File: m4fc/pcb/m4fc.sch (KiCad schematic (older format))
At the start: 70 parts

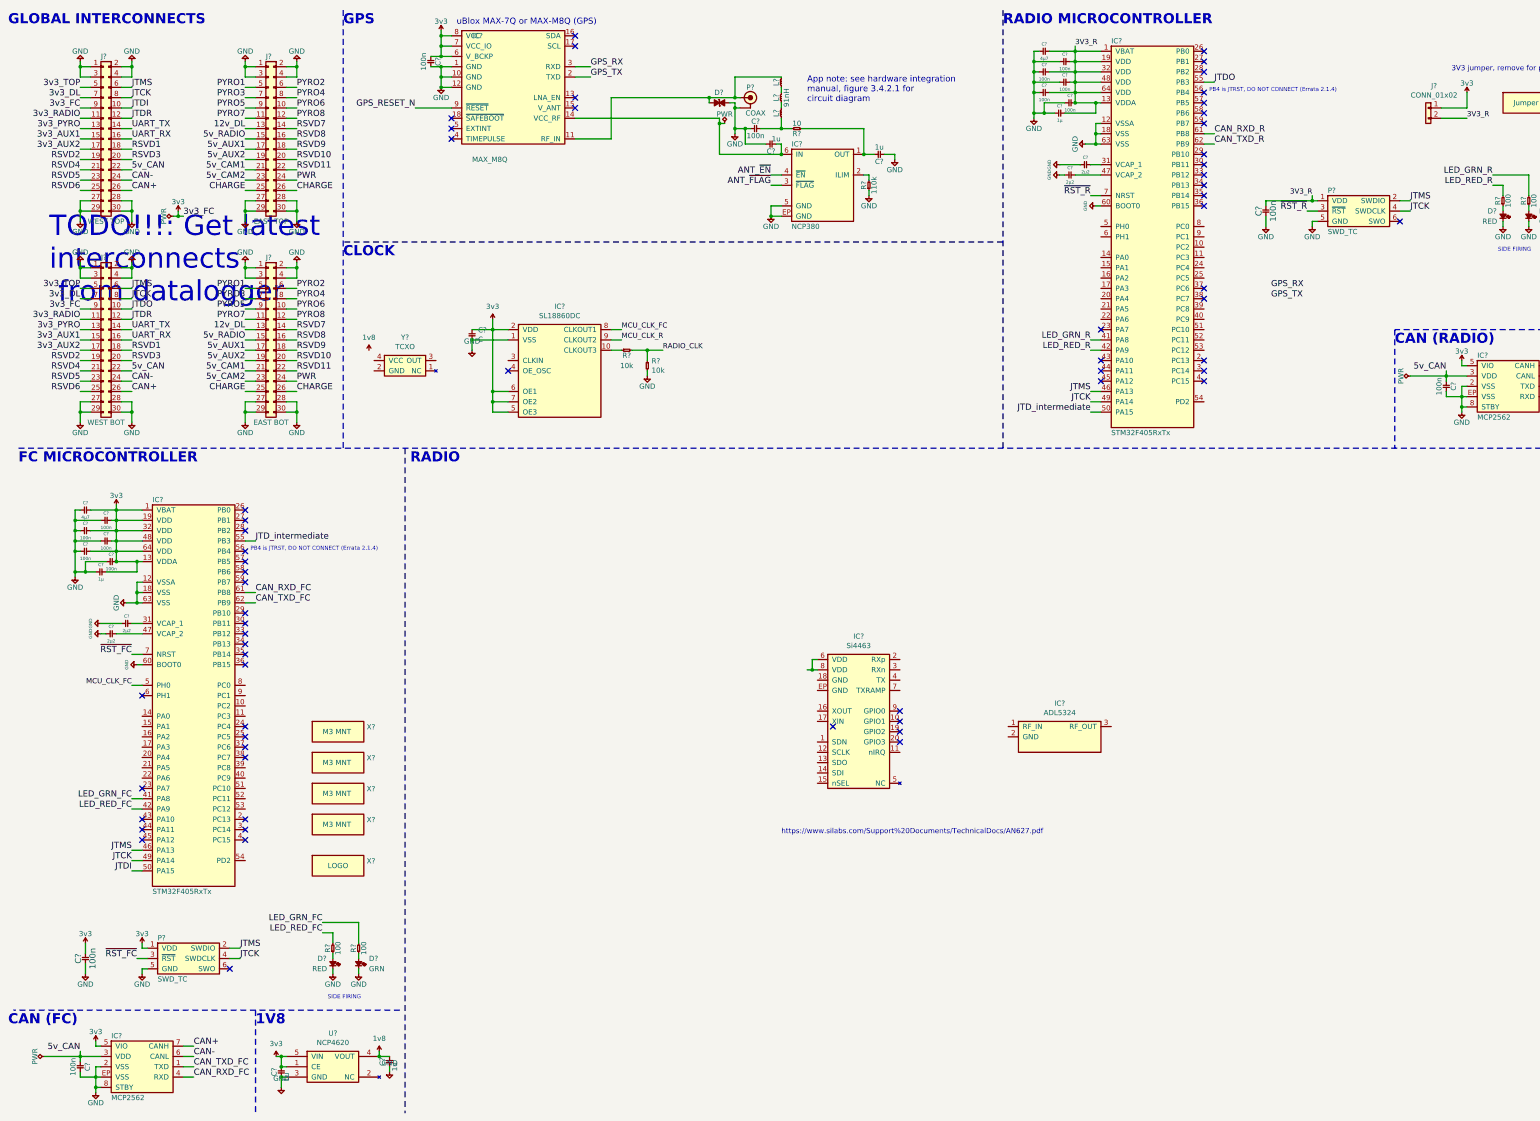
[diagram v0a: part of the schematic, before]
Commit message: Add FC components to schematic
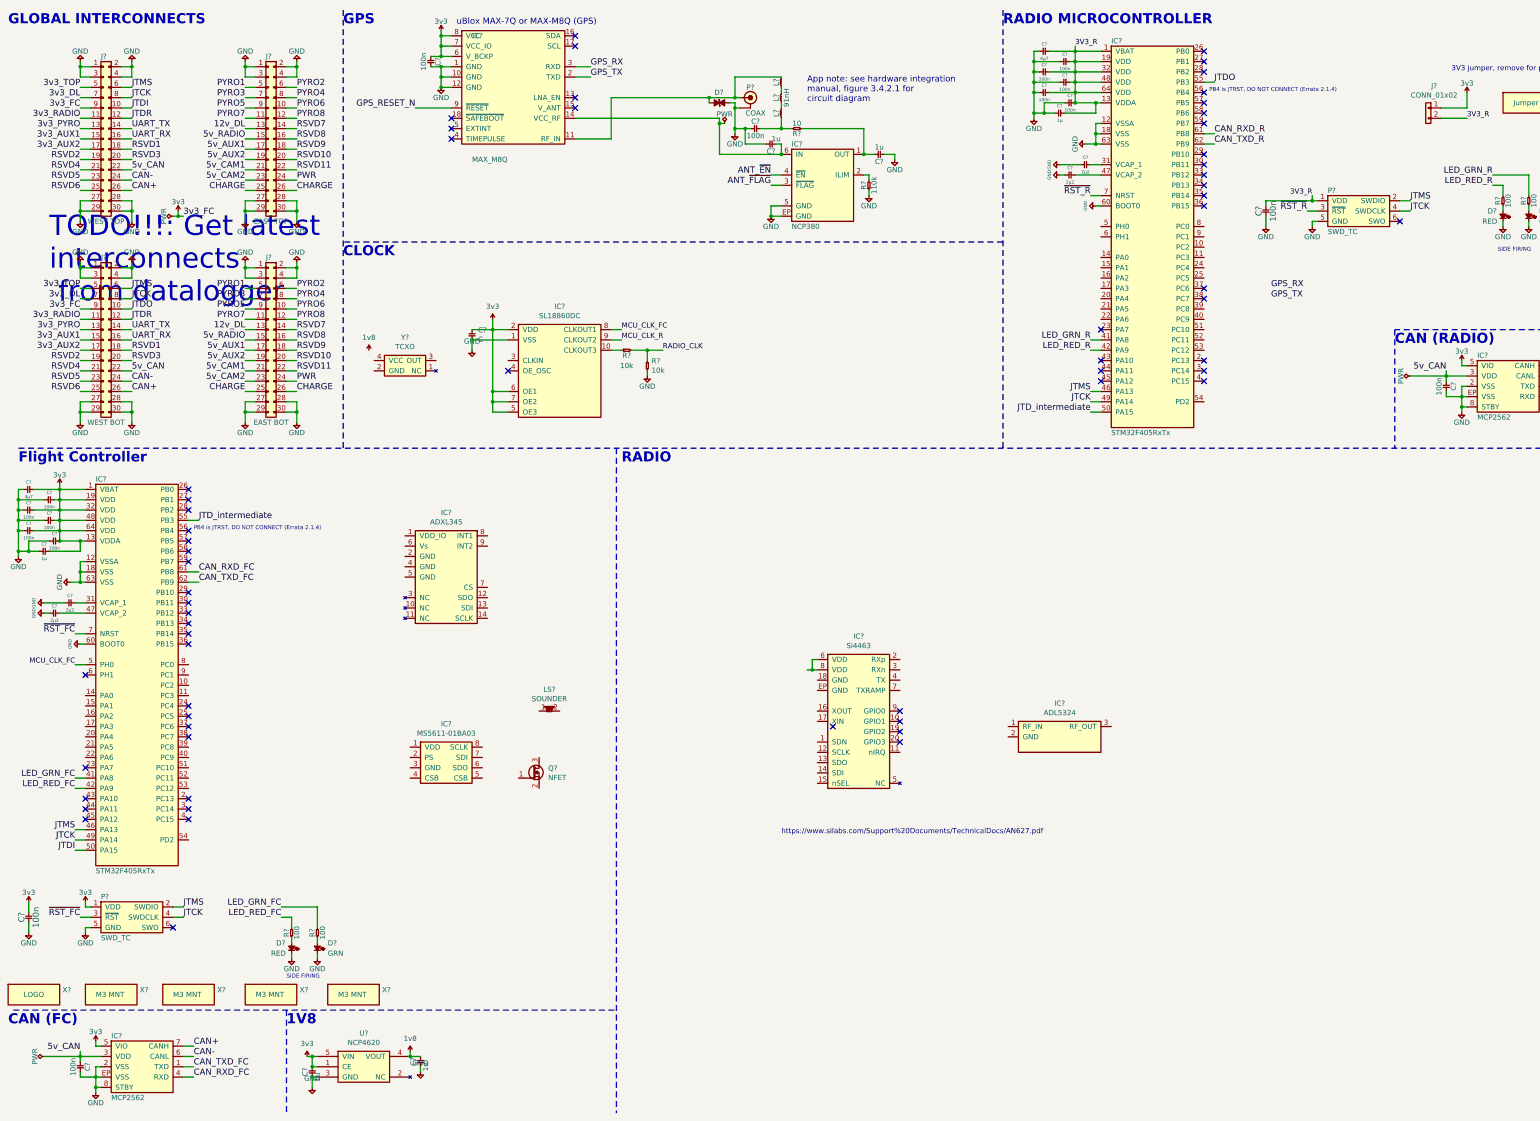
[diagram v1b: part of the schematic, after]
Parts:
- added IC?: ADXL345, agg:ADXL3x5, symbol agg-kicad:ADXL345
- added IC?: MS5611-01BA03, agg:MS5611, symbol agg-kicad:MS5611-01BA03
- added LS?: SOUNDER, symbol agg-kicad:SOUNDER
- added Q?: NFET, agg:SOT-23, symbol agg-kicad:NFET
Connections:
- net 3v3: no longer C?.1, C?.1, C?.1, C?.1, C?.1, C?.1, C?.1, C?.1, C?.1, C?.1, C?.1, C?.1, C?.1, C?.1, C?.1, C?.1, C?.1, C?.1, C?.1, C?.1, C?.2, C?.2, C?.2, C?.2, C?.2, C?.2, C?.2, C?.2, C?.2, D?.1, D?.1, D?.1, D?.1, D?.2, IC?.1 (GND), IC?.1 (VSS), IC?.10 (GND), IC?.12 (GND), IC?.12 (VSSA), IC?.12 (VSSA), IC?.18 (VSS), IC?.18 (VSS), IC?.2 (VSS), IC?.2 (VSS), IC?.5 (GND), IC?.60 (BOOT0), IC?.60 (BOOT0), IC?.63 (VSS), IC?.63 (VSS), IC?.8 (STBY), IC?.8 (STBY), IC?.EP (GND), IC?.EP (VSS), IC?.EP (VSS), J?.1, J?.1, J?.1, J?.1, J?.2, J?.2, J?.2, J?.2, J?.27, J?.27, J?.27, J?.27, J?.28, J?.28, J?.28, J?.28, J?.29, J?.29, J?.29, J?.29, J?.3, J?.3, J?.3, J?.3, J?.30, J?.30, J?.30, J?.30, J?.4, J?.4, J?.4, J?.4, P?.2 (GND), P?.5 (GND), P?.5 (GND), R?.1, R?.2, U?.3 (GND)
- new net GND: C?.1, C?.1, C?.1, C?.1, C?.1, C?.1, C?.1, C?.1, C?.1, C?.1, C?.1, C?.1, C?.1, C?.1, C?.1, C?.1, C?.1, C?.1, C?.1, C?.1, C?.2, C?.2, C?.2, C?.2, C?.2, C?.2, C?.2, C?.2, C?.2, D?.1, D?.1, D?.1, D?.1, D?.2, IC?.1 (GND), IC?.1 (VSS), IC?.10 (GND), IC?.12 (GND), IC?.12 (VSSA), IC?.12 (VSSA), IC?.18 (VSS), IC?.18 (VSS), IC?.2 (VSS), IC?.2 (VSS), IC?.5 (GND), IC?.60 (BOOT0), IC?.60 (BOOT0), IC?.63 (VSS), IC?.63 (VSS), IC?.8 (STBY), IC?.8 (STBY), IC?.EP (GND), IC?.EP (VSS), IC?.EP (VSS), J?.1, J?.1, J?.1, J?.1, J?.2, J?.2, J?.2, J?.2, J?.27, J?.27, J?.27, J?.27, J?.28, J?.28, J?.28, J?.28, J?.29, J?.29, J?.29, J?.29, J?.3, J?.3, J?.3, J?.3, J?.30, J?.30, J?.30, J?.30, J?.4, J?.4, J?.4, J?.4, P?.2 (GND), P?.5 (GND), P?.5 (GND), R?.1, R?.2, U?.3 (GND)
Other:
- note added: "Flight Controller"
- note removed: "FC MICROCONTROLLER"
- moved on the sheet: C?, D?, IC?, P?, R?, U?, X?

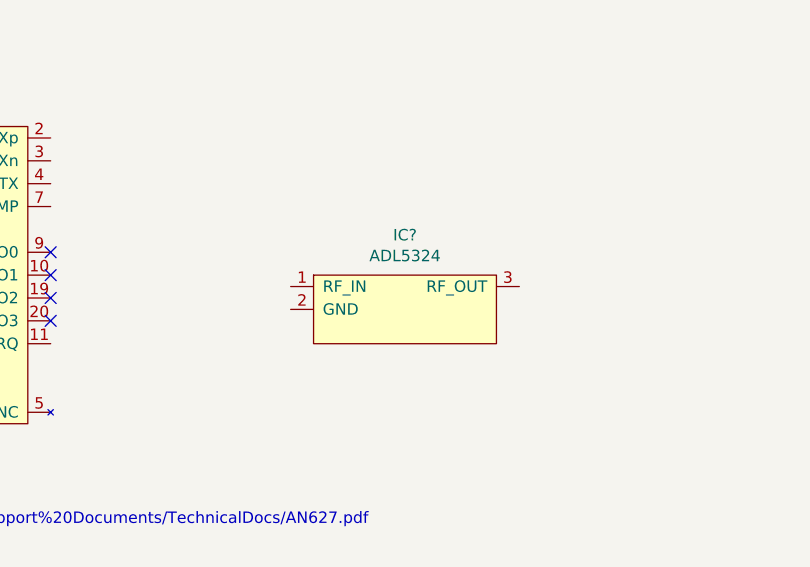
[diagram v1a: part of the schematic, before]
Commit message: Move rf amplifier to separate board
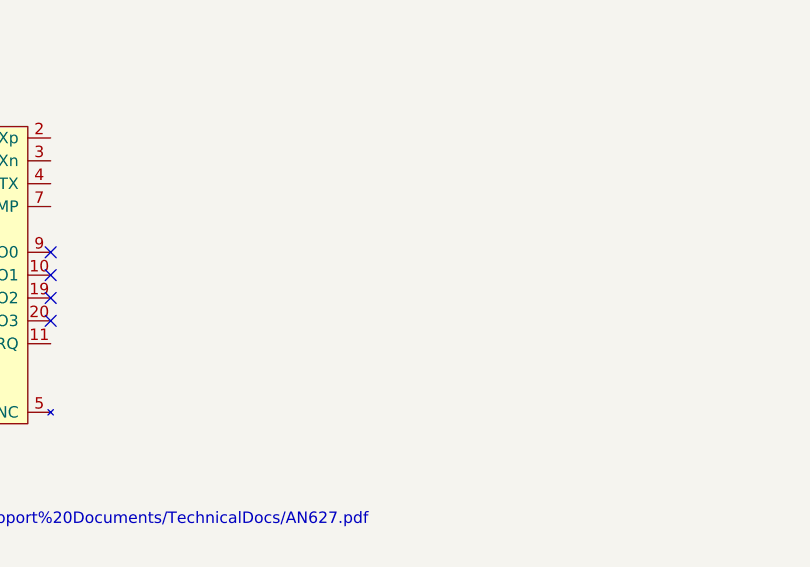
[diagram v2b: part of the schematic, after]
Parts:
- removed IC?: ADL5324, agg:SOT-89-3, symbol agg-kicad:ADL5324
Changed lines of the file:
@@
 Text Notes 6450 4900 0    98   ~ 20
 RADIO
-$Comp
-L agg-kicad:ADL5324 IC?
-U 1 1 5AF6C598
-P 10700 7550
-F 0 "IC?" H 10700 7875 50  0000 C CNN
-F 1 "ADL5324" H 10700 7784 50  0000 C CNN
-F 2 "agg:SOT-89-3" H 10300 7250 50  0001 L CNN
-F 3 "http://www.analog.com/media/en/technical-documentation/data-sheets/ADL5324.pdf" H 10300 7150 50  0001 L CNN
-F 4 "2099794" H 10300 7050 50  0001 L CNN "Farnell"
-	1    10700 7550
-	1    0    0    -1
-$EndComp
 Wire Notes Line
 	550  10200 6400 10200

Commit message: Update clock circuitry and separate 3v3 nets for radio and fc
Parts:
- removed C? (x2): 1u, agg:0402, symbol agg-kicad:C
- removed J?: CONN_01x02, agg:SIL-254P-02, symbol agg-kicad:CONN_01x02
- removed U?: NCP4620, agg:SC-70-5, symbol ncp4620:NCP4620
- removed X?: Jumper, symbol agg-kicad:PART
- added C?: 22n, symbol agg-kicad:C
- added C? (x2): 100n, symbol agg-kicad:C
- added C?: 10n, symbol agg-kicad:C
- added R? (x3): 10k, symbol agg-kicad:R
- added Y?: TCXO, m4fc:2x1.6mm_TCXO, symbol agg-kicad:TCXO
- Y?: footprint (none) -> m4fc:2x1.6mm_TCXO; Farnell 2405785 -> 2545847
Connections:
- net labels added: 3v3_fc, 3v3_radio
- net labels removed: 1v8, 3V3_R, 3v3, MCU_CLK_FC
- wire segments 344 -> 437
- no-connect marks 63 -> 65
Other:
- note added: "Credit gxti\n(https://www.eevblog.com/forum/microcontrollers/stm32-and-external-active-oscillator/)"
- note removed: "1V8"
- note removed: "3V3 jumper, remove for programming"
- moved on the sheet: C?, IC?, R?, Y?
